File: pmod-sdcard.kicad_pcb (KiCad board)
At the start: 4 copper layers, 25.7 x 15.4 mm, 4 parts, among them J1 PMOD_Peripheral_Conn_02x06, J2 Micro_SD_Card

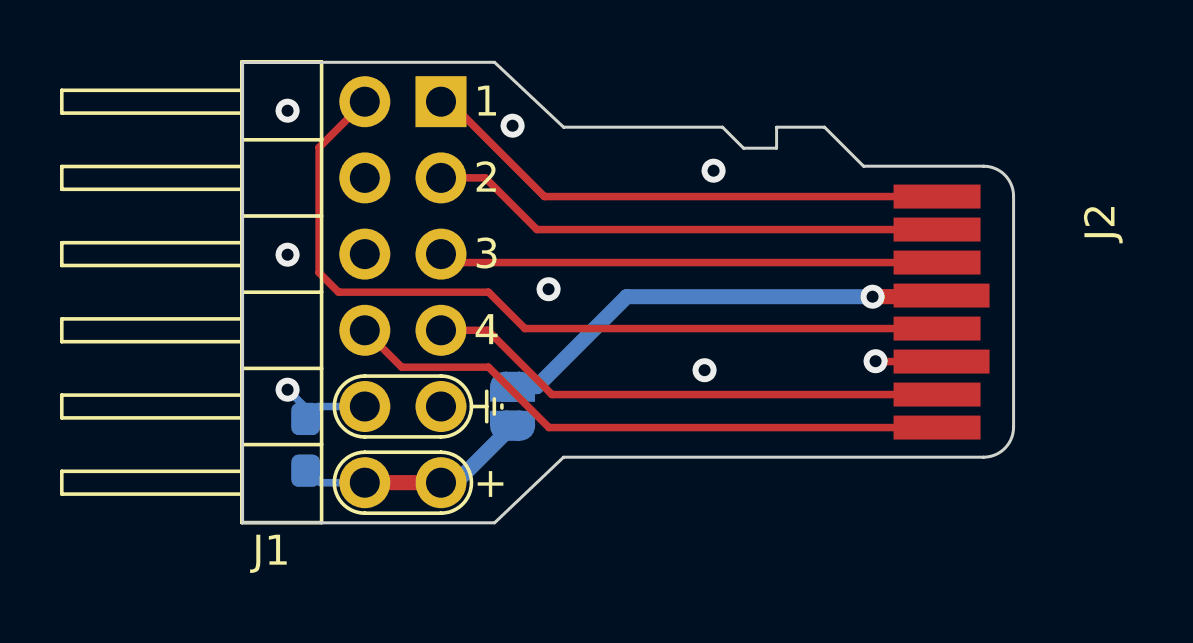
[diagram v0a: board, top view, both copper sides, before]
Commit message: Tweak component placement
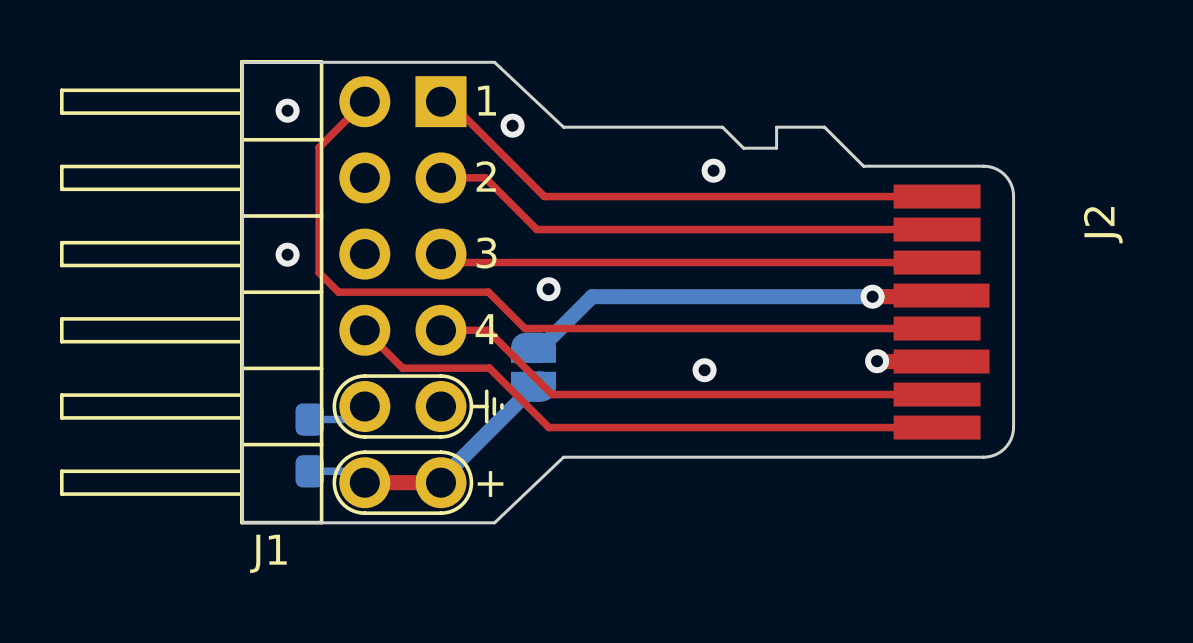
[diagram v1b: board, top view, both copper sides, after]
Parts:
- moved JP1 1.48 mm to (153.2, 72.5)
- moved C1 0.14 mm to (145.7, 75.1)
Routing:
- net VCC: track 8.45 -> 10.1 mm
- net GND: track 5.57 -> 4.27 mm, vias 8 -> 7
- net Net-(J2-Pad4): track 15.6 -> 14.3 mm
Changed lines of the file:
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@@
   )
   (footprint "Capacitor_SMD:C_0603_1608Metric_Pad1.08x0.95mm_HandSolder" (layer "B.Cu")
-    (at 145.6 75.0375 90)
+    (at 145.74 75.0575 90)
     (descr "Capacitor SMD 0603 (1608 Metric), square (rectangular) end terminal, IPC_7351 nominal with elongated pad for handsoldering. (Body size source: IPC-SM-782 page 76, https://www.pcb-3d.com/wordpress/wp-content/uploads/ipc-sm-782a_amendment_1_and_2.pdf), generated with kicad-footprint-generator")
     (tags "capacitor handsolder")
@@
     (property "Sheetname" "")
     (attr smd)
-    (fp_text reference "C1" (at 0.1375 -1.2 90) (layer "B.SilkS")
+    (fp_text reference "C1" (at -0.0225 -1.22 90) (layer "B.SilkS")
       (effects (font (size 1 1) (thickness 0.15)) (justify mirror))
     )
@@
   )
   (footprint "Jumper:SolderJumper-2_P1.3mm_Open_RoundedPad1.0x1.5mm" (layer "B.Cu")
-    (at 152.5 73.75 90)
+    (at 153.2 72.45 90)
     (descr "SMD Solder Jumper, 1x1.5mm, rounded Pads, 0.3mm gap, open")
     (tags "solder jumper open")
@@
     (property "Sheetname" "")
     (attr exclude_from_pos_files)
-    (fp_text reference "JP1" (at 0.118503 1.918503 90) (layer "B.SilkS") hide
+    (fp_text reference "JP1" (at 0.118503 1.918503 270) (layer "B.SilkS") hide
       (effects (font (size 1 1) (thickness 0.15)) (justify mirror))
     )
-    (fp_text value "3V3" (at 0 3.05 180) (layer "B.SilkS")
+    (fp_text value "3V3" (at -0.05 1.85 90) (layer "B.SilkS")
       (effects (font (size 1 1) (thickness 0.15)) (justify mirror))
     )
-    (fp_line (start -1.4 -0.3) (end -1.4 0.3) (layer "B.SilkS") (width 0.12))
-    (fp_line (start 0.7 -1) (end -0.7 -1) (layer "B.SilkS") (width 0.12))
-    (fp_line (start -0.7 1) (end 0.7 1) (layer "B.SilkS") (width 0.12))
-    (fp_line (start 1.4 0.3) (end 1.4 -0.3) (layer "B.SilkS") (width 0.12))
-    (fp_arc (start -0.7 1) (mid -1.194975 0.794975) (end -1.4 0.3) (layer "B.SilkS") (width 0.12))
-    (fp_arc (start 1.4 0.3) (mid 1.194975 0.794975) (end 0.7 1) (layer "B.SilkS") (width 0.12))
-    (fp_arc (start 0.7 -1) (mid 1.194975 -0.794975) (end 1.4 -0.3) (layer "B.SilkS") (width 0.12))
-    (fp_arc (start -1.4 -0.3) (mid -1.194975 -0.794975) (end -0.7 -1) (layer "B.SilkS") (width 0.12))
     (fp_line (start 1.65 -1.25) (end -1.65 -1.25) (layer "B.CrtYd") (width 0.05))
     (fp_line (start 1.65 -1.25) (end 1.65 1.25) (layer "B.CrtYd") (width 0.05))
@@
   (gr_line (start 161.3 64.45) (end 162.9 64.45) (layer "Edge.Cuts") (width 0.1))
   (gr_line (start 162.9 64.45) (end 164.2 65.75) (layer "Edge.Cuts") (width 0.1))
-  (segment (start 166.8 72.262) (end 164.612 72.262) (width 0.25) (layer "F.Cu") (net 1))
-  (segment (start 164.612 72.262) (end 164.6 72.25) (width 0.25) (layer "F.Cu") (net 1))
+  (segment (start 164.662 72.262) (end 166.8 72.262) (width 0.5) (layer "F.Cu") (net 1))
+  (segment (start 164.65 72.25) (end 164.662 72.262) (width 0.5) (layer "F.Cu") (net 1))
+  (via (at 164.65 72.25) (size 0.8) (drill 0.4) (layers "F.Cu" "B.Cu") (net 1))
   (via (at 159.2 65.9) (size 0.8) (drill 0.4) (layers "F.Cu" "B.Cu") (free) (net 1))
   (via (at 158.9 72.55) (size 0.8) (drill 0.4) (layers "F.Cu" "B.Cu") (free) (net 1))
   (via (at 152.5 64.4) (size 0.8) (drill 0.4) (layers "F.Cu" "B.Cu") (free) (net 1))
-  (via (at 164.6 72.25) (size 0.8) (drill 0.4) (layers "F.Cu" "B.Cu") (net 1))
   (via (at 145 63.9) (size 0.8) (drill 0.4) (layers "F.Cu" "B.Cu") (free) (net 1))
   (via (at 153.7 69.85) (size 0.8) (drill 0.4) (layers "F.Cu" "B.Cu") (free) (net 1))
   (via (at 145 68.7) (size 0.8) (drill 0.4) (layers "F.Cu" "B.Cu") (free) (net 1))
-  (via (at 145 73.2) (size 0.8) (drill 0.4) (layers "F.Cu" "B.Cu") (net 1))
-  (segment (start 146.015 73.76) (end 145.6 74.175) (width 0.25) (layer "B.Cu") (net 1))
-  (segment (start 145.6 74.175) (end 145.6 73.8) (width 0.25) (layer "B.Cu") (net 1))
-  (segment (start 145.6 73.8) (end 145 73.2) (width 0.25) (layer "B.Cu") (net 1))
-  (segment (start 147.574 73.76) (end 146.015 73.76) (width 0.25) (layer "B.Cu") (net 1))
+  (segment (start 145.6 74.175) (end 145.67 74.105) (width 0.25) (layer "B.Cu") (net 1))
+  (segment (start 145.74 74.195) (end 147.139 74.195) (width 0.25) (layer "B.Cu") (net 1))
+  (segment (start 147.139 74.195) (end 147.574 73.76) (width 0.25) (layer "B.Cu") (net 1))
   (segment (start 147.574 76.3) (end 150.114 76.3) (width 0.5) (layer "F.Cu") (net 2))
   (segment (start 150.114 76.3) (end 150.7 76.3) (width 0.5) (layer "B.Cu") (net 2))
-  (segment (start 145.6 75.9) (end 145.7 75.9) (width 0.25) (layer "B.Cu") (net 2))
-  (segment (start 150.6 76.3) (end 152.5 74.4) (width 0.5) (layer "B.Cu") (net 2))
-  (segment (start 145.7 75.9) (end 146.1 76.3) (width 0.25) (layer "B.Cu") (net 2))
-  (segment (start 150.114 76.3) (end 150.114 76.286) (width 0.5) (layer "B.Cu") (net 2))
-  (segment (start 146.1 76.3) (end 147.574 76.3) (width 0.25) (layer "B.Cu") (net 2))
+  (segment (start 147.194 75.92) (end 147.574 76.3) (width 0.25) (layer "B.Cu") (net 2))
+  (segment (start 150.114 76.186) (end 153.2 73.1) (width 0.5) (layer "B.Cu") (net 2))
+  (segment (start 150.114 76.3) (end 150.114 76.186) (width 0.5) (layer "B.Cu") (net 2))
+  (segment (start 145.74 75.92) (end 147.194 75.92) (width 0.25) (layer "B.Cu") (net 2))
   (segment (start 150.114 76.3) (end 150.6 76.3) (width 0.5) (layer "B.Cu") (net 2))
   (segment (start 146.05 69.3) (end 146.05 65.124) (width 0.25) (layer "F.Cu") (net 3))
@@
   (segment (start 151.67 71.22) (end 153.812 73.362) (width 0.25) (layer "F.Cu") (net 6))
   (segment (start 150.114 71.22) (end 151.67 71.22) (width 0.25) (layer "F.Cu") (net 6))
+  (segment (start 148.834 72.48) (end 151.73 72.48) (width 0.25) (layer "F.Cu") (net 7))
   (segment (start 153.712 74.462) (end 166.65 74.462) (width 0.25) (layer "F.Cu") (net 7))
-  (segment (start 151.7 72.45) (end 153.712 74.462) (width 0.25) (layer "F.Cu") (net 7))
-  (segment (start 147.574 71.22) (end 148.804 72.45) (width 0.25) (layer "F.Cu") (net 7))
-  (segment (start 148.804 72.45) (end 151.7 72.45) (width 0.25) (layer "F.Cu") (net 7))
+  (segment (start 151.73 72.48) (end 153.712 74.462) (width 0.25) (layer "F.Cu") (net 7))
+  (segment (start 147.574 71.22) (end 148.834 72.48) (width 0.25) (layer "F.Cu") (net 7))
+  (segment (start 166.65 68.962) (end 150.396 68.962) (width 0.25) (layer "F.Cu") (net 8))
   (segment (start 150.396 68.962) (end 150.114 68.68) (width 0.25) (layer "F.Cu") (net 8))
-  (segment (start 166.65 68.962) (end 150.396 68.962) (width 0.25) (layer "F.Cu") (net 8))
   (segment (start 164.5 70.1) (end 166.762 70.1) (width 0.5) (layer "F.Cu") (net 11))
   (segment (start 166.762 70.1) (end 166.8 70.062) (width 0.5) (layer "F.Cu") (net 11))
   (via (at 164.5 70.1) (size 0.8) (drill 0.4) (layers "F.Cu" "B.Cu") (net 11))
-  (segment (start 164.5 70.1) (end 156.3 70.1) (width 0.5) (layer "B.Cu") (net 11))
-  (segment (start 156.3 70.1) (end 153.3 73.1) (width 0.5) (layer "B.Cu") (net 11))
-  (segment (start 153.3 73.1) (end 152.5 73.1) (width 0.5) (layer "B.Cu") (net 11))
+  (segment (start 153.2 71.8) (end 153.45 71.8) (width 0.5) (layer "B.Cu") (net 11))
+  (segment (start 155.15 70.1) (end 164.5 70.1) (width 0.5) (layer "B.Cu") (net 11))
+  (segment (start 153.45 71.8) (end 155.15 70.1) (width 0.5) (layer "B.Cu") (net 11))
   (zone (net 1) (net_name "GND") (layer "In1.Cu") (hatch edge 0.508)
     (connect_pads (clearance 0.25))

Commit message: Run DRC and fix warnings
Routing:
- net VCC: track 10.1 -> 9.01 mm
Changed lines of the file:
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@@
   (via (at 153.7 69.85) (size 0.8) (drill 0.4) (layers "F.Cu" "B.Cu") (free) (net 1))
   (via (at 145 68.7) (size 0.8) (drill 0.4) (layers "F.Cu" "B.Cu") (free) (net 1))
-  (segment (start 145.6 74.175) (end 145.67 74.105) (width 0.25) (layer "B.Cu") (net 1))
   (segment (start 145.74 74.195) (end 147.139 74.195) (width 0.25) (layer "B.Cu") (net 1))
   (segment (start 147.139 74.195) (end 147.574 73.76) (width 0.25) (layer "B.Cu") (net 1))
   (segment (start 147.574 76.3) (end 150.114 76.3) (width 0.5) (layer "F.Cu") (net 2))
-  (segment (start 150.114 76.3) (end 150.7 76.3) (width 0.5) (layer "B.Cu") (net 2))
   (segment (start 147.194 75.92) (end 147.574 76.3) (width 0.25) (layer "B.Cu") (net 2))
   (segment (start 150.114 76.186) (end 153.2 73.1) (width 0.5) (layer "B.Cu") (net 2))
   (segment (start 150.114 76.3) (end 150.114 76.186) (width 0.5) (layer "B.Cu") (net 2))
   (segment (start 145.74 75.92) (end 147.194 75.92) (width 0.25) (layer "B.Cu") (net 2))
-  (segment (start 150.114 76.3) (end 150.6 76.3) (width 0.5) (layer "B.Cu") (net 2))
   (segment (start 146.05 69.3) (end 146.05 65.124) (width 0.25) (layer "F.Cu") (net 3))
   (segment (start 166.65 71.162) (end 152.912 71.162) (width 0.25) (layer "F.Cu") (net 3))

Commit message: Check in gerbers
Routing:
- net CLK: track 27.7 -> 24.8 mm
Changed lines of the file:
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@@
       (layerselection 0x00010fc_ffffffff)
       (disableapertmacros false)
-      (usegerberextensions false)
+      (usegerberextensions true)
       (usegerberattributes true)
       (usegerberadvancedattributes true)
-      (creategerberjobfile true)
+      (creategerberjobfile false)
       (svguseinch false)
       (svgprecision 6)
@@
       (psa4output false)
       (plotreference true)
-      (plotvalue true)
+      (plotvalue false)
       (plotinvisibletext false)
       (sketchpadsonfab false)
-      (subtractmaskfromsilk false)
+      (subtractmaskfromsilk true)
       (outputformat 1)
       (mirror false)
-      (drillshape 1)
+      (drillshape 0)
       (scaleselection 1)
-      (outputdirectory "")
+      (outputdirectory "pmod-sdcard-gerbers")
     )
   )
@@
   (segment (start 150.114 76.3) (end 150.114 76.186) (width 0.5) (layer "B.Cu") (net 2))
   (segment (start 145.74 75.92) (end 147.194 75.92) (width 0.25) (layer "B.Cu") (net 2))
-  (segment (start 146.05 69.3) (end 146.05 65.124) (width 0.25) (layer "F.Cu") (net 3))
-  (segment (start 166.65 71.162) (end 152.912 71.162) (width 0.25) (layer "F.Cu") (net 3))
-  (segment (start 152.912 71.162) (end 151.7 69.95) (width 0.25) (layer "F.Cu") (net 3))
-  (segment (start 151.7 69.95) (end 146.7 69.95) (width 0.25) (layer "F.Cu") (net 3))
-  (segment (start 146.05 65.124) (end 147.574 63.6) (width 0.25) (layer "F.Cu") (net 3))
-  (segment (start 146.7 69.95) (end 146.05 69.3) (width 0.25) (layer "F.Cu") (net 3))
+  (segment (start 147.574 63.6) (end 148.85 64.876) (width 0.25) (layer "F.Cu") (net 3))
+  (segment (start 148.85 69.25) (end 149.55 69.95) (width 0.25) (layer "F.Cu") (net 3))
+  (segment (start 149.55 69.95) (end 151.7 69.95) (width 0.25) (layer "F.Cu") (net 3))
+  (segment (start 151.7 69.95) (end 152.912 71.162) (width 0.25) (layer "F.Cu") (net 3))
+  (segment (start 152.912 71.162) (end 166.65 71.162) (width 0.25) (layer "F.Cu") (net 3))
+  (segment (start 148.85 64.876) (end 148.85 69.25) (width 0.25) (layer "F.Cu") (net 3))
   (segment (start 153.562 66.762) (end 150.4 63.6) (width 0.25) (layer "F.Cu") (net 4))
   (segment (start 150.4 63.6) (end 150.114 63.6) (width 0.25) (layer "F.Cu") (net 4))

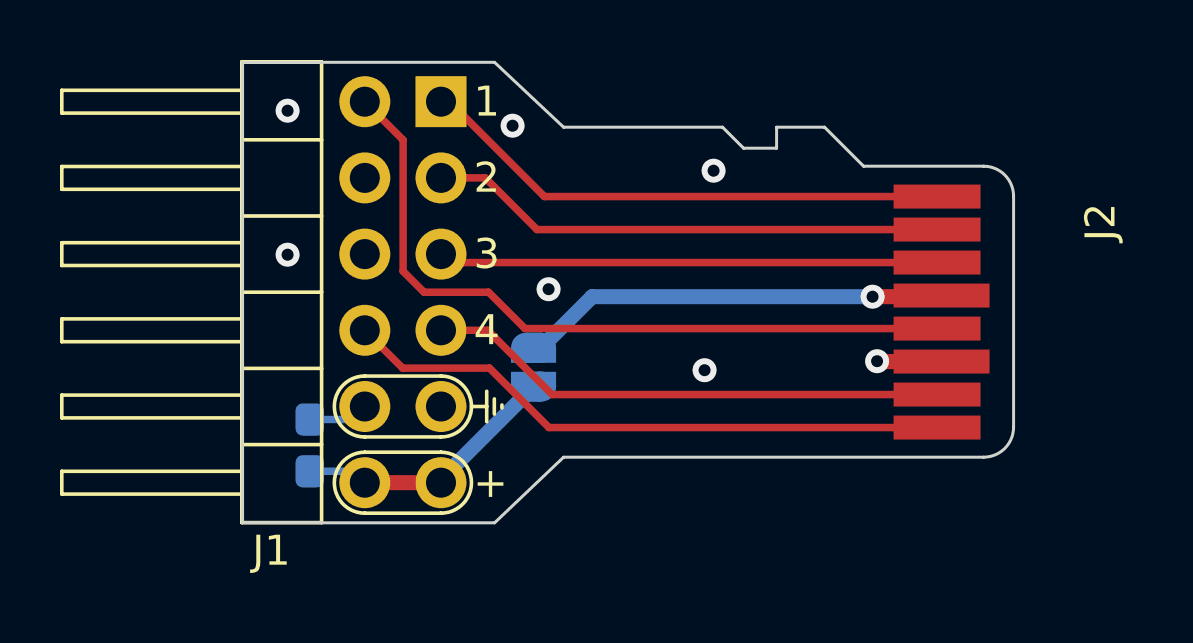
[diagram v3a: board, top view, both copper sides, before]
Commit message: Add series resistors for signal lines
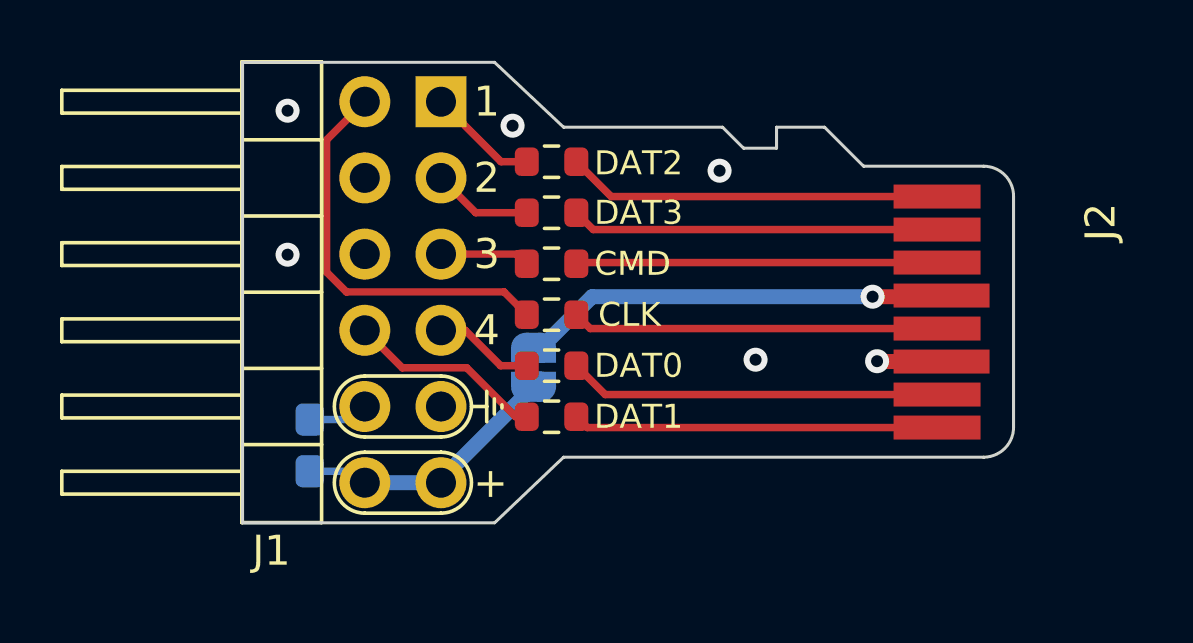
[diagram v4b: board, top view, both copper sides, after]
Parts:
- added R1: 30, Resistor_SMD:R_0603_1608Metric, F.Cu at (153.8, 65.6)
- added R2: 30, Resistor_SMD:R_0603_1608Metric, F.Cu at (153.8, 67.3)
- added R3: 30, Resistor_SMD:R_0603_1608Metric, F.Cu at (153.8, 69.0)
- added R4: 30, Resistor_SMD:R_0603_1608Metric, F.Cu at (153.8, 72.4)
- added R5: 30, Resistor_SMD:R_0603_1608Metric, F.Cu at (153.8, 70.7)
- added R6: 30, Resistor_SMD:R_0603_1608Metric, F.Cu at (153.8, 74.1)
- added REF**: OSHW-Symbol_6.7x6mm_SilkScreen, Symbol:OSHW-Symbol_6.7x6mm_SilkScreen, B.Cu at (160.6, 70.4)
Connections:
- J1 pad 1: DAT2 -> Net-(J1-Pad1)
- J1 pad 10: DAT1 -> Net-(J1-Pad10)
- J1 pad 2: DAT3 -> Net-(J1-Pad2)
- J1 pad 3: CMD -> Net-(J1-Pad3)
- J1 pad 4: DAT0 -> Net-(J1-Pad4)
- J1 pad 7: CLK -> Net-(J1-Pad7)
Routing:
- net Net-(J1-Pad7): track 0.00 -> 13.5 mm
- net CLK: track 24.8 -> 12.2 mm
- net DAT1: track 20.4 -> 12.2 mm
- net Net-(J1-Pad10): track 0.00 -> 6.59 mm
- net DAT2: track 17.8 -> 12.5 mm
- net DAT0: track 17.4 -> 12.4 mm
- net DAT3: track 17.2 -> 12.3 mm
- net CMD: track 16.7 -> 12.0 mm
- net Net-(J1-Pad1): track 0.00 -> 3.69 mm
- net Net-(J1-Pad4): track 0.00 -> 3.35 mm
- net Net-(J1-Pad2): track 0.00 -> 3.34 mm
- net Net-(J1-Pad3): track 0.00 -> 2.99 mm
- net GND: vias 7 -> 6
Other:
- board text added: "CLK"
- board text added: "CMD"
- board text added: "DAT0"
- board text added: "DAT1"
- board text added: "DAT2"
- board text added: "DAT3"
